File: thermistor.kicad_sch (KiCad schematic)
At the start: 2 parts

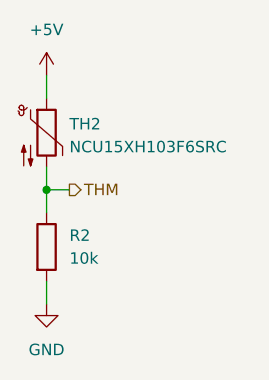
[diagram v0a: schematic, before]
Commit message: Change last end to 0 from 17
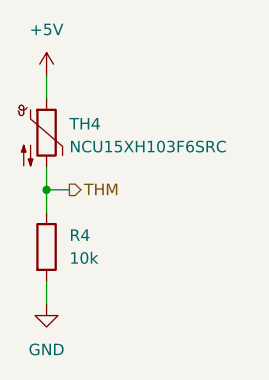
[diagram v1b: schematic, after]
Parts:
- renumbered R2 to R4, TH2 to TH4
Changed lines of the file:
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@@
 		(dnp no)
 		(fields_autoplaced yes)
-		(property "Reference" "#PWR04"
+		(property "Reference" "#PWR08"
 			(at 88.9 92.71 0)
 			(effects
@@
 		(dnp no)
 		(fields_autoplaced yes)
-		(property "Reference" "#PWR03"
+		(property "Reference" "#PWR07"
 			(at 88.9 64.77 0)
 			(effects
@@
 		(dnp no)
 		(fields_autoplaced yes)
-		(property "Reference" "TH2"
+		(property "Reference" "TH4"
 			(at 91.44 66.3574 0)
 			(effects
@@
 		(dnp no)
 		(fields_autoplaced yes)
-		(property "Reference" "R2"
+		(property "Reference" "R4"
 			(at 91.44 78.7399 0)
 			(effects
